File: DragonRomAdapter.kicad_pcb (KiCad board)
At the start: 2 copper layers, 20.6 x 36.9 mm, 8 parts, among them J1 Conn_01x01_Male, U1 68A364, U2 74LVC1G00, U3 28C256

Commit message: tidy-up board
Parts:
- added JP2: Jumper_2_Open, Jumper:SolderJumper-2_P1.3mm_Open_TrianglePad1.0x1.5mm, F.Cu at (165.5, 64.8)
- moved R3 0.71 mm to (160.4, 85.3)
- moved JP1 0.51 mm to (166.5, 88.0)
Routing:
- net GND: track 8.63 -> 30.0 mm, vias 0 -> 2
- net ~{E17}: track 24.5 -> 35.1 mm, vias 0 -> 3
- net ~{E}: track 15.4 -> 19.8 mm, vias 0 -> 1
- net Net-(JP1-Pad1): track 3.44 -> 2.93 mm
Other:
- board text added: "Dragon ROM adapter"
- board text added: "created by Julian Brown"

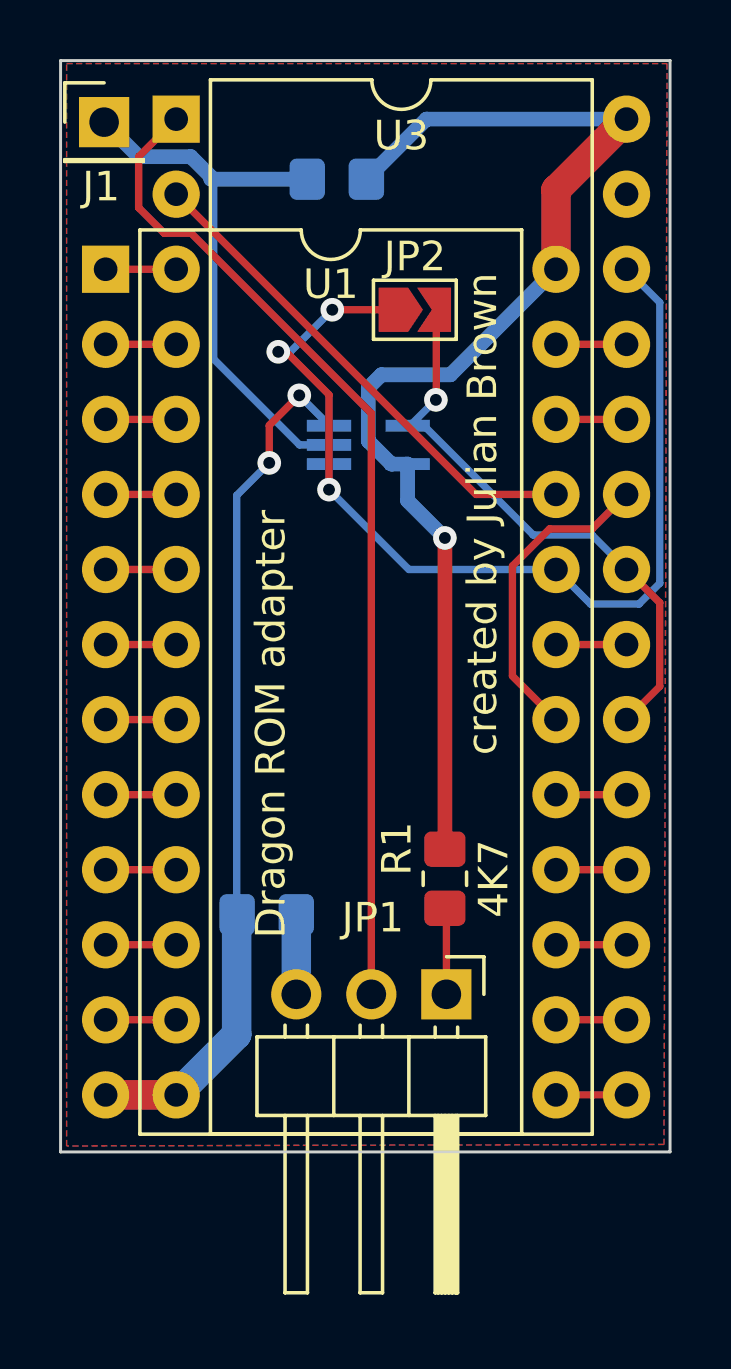
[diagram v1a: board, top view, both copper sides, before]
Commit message: reduce size of board to fit some main boards
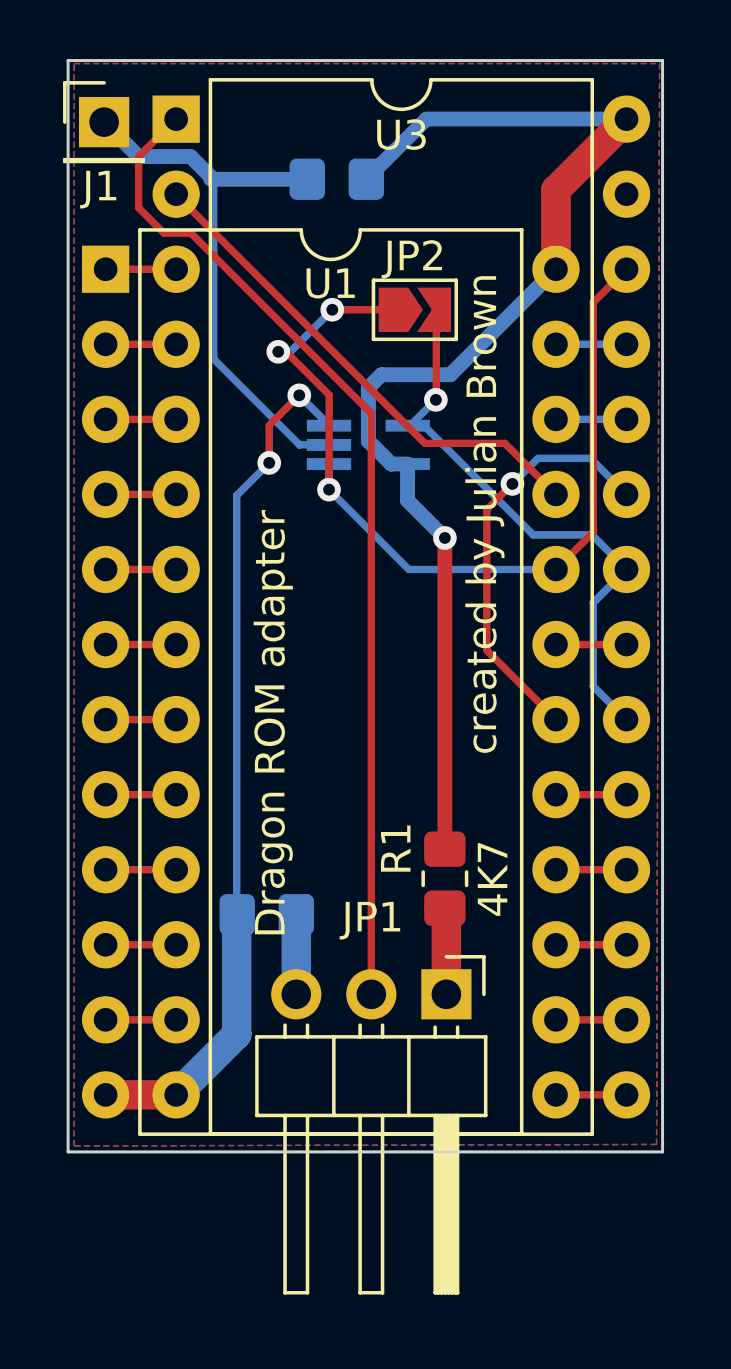
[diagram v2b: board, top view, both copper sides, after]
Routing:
- net ~{E17}: track 35.1 -> 30.8 mm
- net A11: track 10.7 -> 14.0 mm, vias 0 -> 1
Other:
- board size 20.6 x 36.9 mm -> 20.1 x 36.9 mm
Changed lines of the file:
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@@
     )
   )
-  (gr_rect (start 153.4668 56.388) (end 174.0916 93.3196) (layer "Edge.Cuts") (width 0.1) (fill none))
+  (gr_rect (start 153.7208 56.388) (end 173.8376 93.3196) (layer "Edge.Cuts") (width 0.1) (fill none))
   (gr_text "created by Julian Brown" (at 167.7416 71.7296 90) (layer "F.SilkS")
     (effects (font (size 1 1) (thickness 0.15)))
@@
   (segment (start 170.2308 81.2292) (end 172.6034 81.2292) (width 0.25) (layer "F.Cu") (net 17))
   (segment (start 172.6034 81.2292) (end 172.6134 81.2392) (width 0.25) (layer "F.Cu") (net 17))
-  (segment (start 168.7576 73.4921) (end 168.7576 77.216) (width 0.25) (layer "F.Cu") (net 18))
-  (segment (start 168.7576 77.216) (end 170.2308 78.6892) (width 0.25) (layer "F.Cu") (net 18))
-  (segment (start 171.455 72.2376) (end 170.0121 72.2376) (width 0.25) (layer "F.Cu") (net 18))
-  (segment (start 172.6134 71.0792) (end 171.455 72.2376) (width 0.25) (layer "F.Cu") (net 18))
-  (segment (start 170.0121 72.2376) (end 168.7576 73.4921) (width 0.25) (layer "F.Cu") (net 18))
+  (segment (start 167.894 71.5772) (end 167.894 76.3524) (width 0.25) (layer "F.Cu") (net 18))
+  (segment (start 167.894 76.3524) (end 170.2308 78.6892) (width 0.25) (layer "F.Cu") (net 18))
+  (segment (start 168.7576 70.7136) (end 167.894 71.5772) (width 0.25) (layer "F.Cu") (net 18))
+  (via (at 168.7576 70.7136) (size 0.8) (drill 0.4) (layers "F.Cu" "B.Cu") (net 18))
+  (segment (start 168.7576 70.7136) (end 169.6212 69.85) (width 0.25) (layer "B.Cu") (net 18))
+  (segment (start 169.6212 69.85) (end 171.3992 69.85) (width 0.25) (layer "B.Cu") (net 18))
+  (segment (start 171.3992 69.85) (end 172.6184 71.0692) (width 0.25) (layer "B.Cu") (net 18))
   (segment (start 170.2308 76.1492) (end 172.6034 76.1492) (width 0.25) (layer "F.Cu") (net 19))
   (segment (start 172.6034 76.1492) (end 172.6134 76.1592) (width 0.25) (layer "F.Cu") (net 19))
-  (segment (start 173.742911 74.733711) (end 173.742911 77.564689) (width 0.25) (layer "F.Cu") (net 20))
-  (segment (start 172.6184 73.6092) (end 173.742911 74.733711) (width 0.25) (layer "F.Cu") (net 20))
-  (segment (start 173.742911 77.564689) (end 172.6184 78.6892) (width 0.25) (layer "F.Cu") (net 20))
   (segment (start 166.1806 67.855389) (end 166.1806 64.8208) (width 0.25) (layer "F.Cu") (net 20))
   (segment (start 166.1668 67.869189) (end 166.1806 67.855389) (width 0.25) (layer "F.Cu") (net 20))
   (via (at 166.1668 67.869189) (size 0.8) (drill 0.4) (layers "F.Cu" "B.Cu") (net 20))
+  (segment (start 171.4934 74.7342) (end 172.6184 73.6092) (width 0.25) (layer "B.Cu") (net 20))
+  (segment (start 172.6184 78.6892) (end 171.4934 77.5642) (width 0.25) (layer "B.Cu") (net 20))
   (segment (start 165.2108 68.7428) (end 165.7608 68.7428) (width 0.25) (layer "B.Cu") (net 20))
   (segment (start 171.45 72.4408) (end 172.6184 73.6092) (width 0.25) (layer "B.Cu") (net 20))
@@
   (segment (start 165.293189 68.7428) (end 166.1668 67.869189) (width 0.25) (layer "B.Cu") (net 20))
   (segment (start 169.4588 72.4408) (end 171.45 72.4408) (width 0.25) (layer "B.Cu") (net 20))
-  (segment (start 170.2308 71.0692) (end 167.5234 71.0692) (width 0.25) (layer "F.Cu") (net 21))
-  (segment (start 167.5234 71.0692) (end 157.3734 60.9192) (width 0.25) (layer "F.Cu") (net 21))
-  (segment (start 170.2308 68.5292) (end 172.6034 68.5292) (width 0.25) (layer "F.Cu") (net 22))
-  (segment (start 172.6034 68.5292) (end 172.6134 68.5392) (width 0.25) (layer "F.Cu") (net 22))
-  (segment (start 172.6034 65.9892) (end 172.6134 65.9992) (width 0.25) (layer "F.Cu") (net 23))
-  (segment (start 170.2308 65.9892) (end 172.6034 65.9892) (width 0.25) (layer "F.Cu") (net 23))
+  (segment (start 171.4934 77.5642) (end 171.4934 74.7342) (width 0.25) (layer "B.Cu") (net 20))
+  (segment (start 165.7962 69.342) (end 157.3734 60.9192) (width 0.25) (layer "F.Cu") (net 21))
+  (segment (start 170.2308 71.0692) (end 168.5036 69.342) (width 0.25) (layer "F.Cu") (net 21))
+  (segment (start 168.5036 69.342) (end 165.7962 69.342) (width 0.25) (layer "F.Cu") (net 21))
+  (segment (start 170.2308 68.5292) (end 172.6184 68.5292) (width 0.25) (layer "B.Cu") (net 22))
+  (segment (start 170.2308 65.9892) (end 172.6184 65.9892) (width 0.25) (layer "B.Cu") (net 23))
   (segment (start 170.2308 63.4492) (end 170.2308 60.7618) (width 1) (layer "F.Cu") (net 24))
   (segment (start 166.4716 72.5424) (end 166.4716 83.074) (width 0.5) (layer "F.Cu") (net 24))
@@
   (segment (start 161.5508 69.3928) (end 162.5508 69.3928) (width 0.25) (layer "B.Cu") (net 25))
   (segment (start 166.4716 85.074) (end 166.5224 85.1248) (width 0.25) (layer "F.Cu") (net 26))
-  (segment (start 166.5224 85.1248) (end 166.5224 87.9856) (width 0.25) (layer "F.Cu") (net 26))
+  (segment (start 166.5224 85.1248) (end 166.5224 87.9856) (width 1) (layer "F.Cu") (net 26))
   (segment (start 156.1084 61.3664) (end 156.972 62.23) (width 0.25) (layer "F.Cu") (net 27))
   (segment (start 157.3784 58.3692) (end 156.1084 59.6392) (width 0.25) (layer "F.Cu") (net 27))
@@
   (segment (start 156.1084 59.6392) (end 156.1084 61.3664) (width 0.25) (layer "F.Cu") (net 27))
   (segment (start 163.9824 68.326) (end 163.9824 87.9856) (width 0.25) (layer "F.Cu") (net 27))
+  (segment (start 171.4934 64.5742) (end 171.4934 72.3466) (width 0.25) (layer "F.Cu") (net 28))
+  (segment (start 171.4934 72.3466) (end 170.2308 73.6092) (width 0.25) (layer "F.Cu") (net 28))
   (segment (start 162.6616 64.8208) (end 164.7306 64.8208) (width 0.25) (layer "F.Cu") (net 28))
+  (segment (start 172.6184 63.4492) (end 171.4934 64.5742) (width 0.25) (layer "F.Cu") (net 28))
   (segment (start 161.095414 66.2432) (end 160.8328 66.2432) (width 0.25) (layer "F.Cu") (net 28))
   (segment (start 162.5508 67.698586) (end 161.095414 66.2432) (width 0.25) (layer "F.Cu") (net 28))
@@
   (via (at 162.5508 70.9076) (size 0.8) (drill 0.4) (layers "F.Cu" "B.Cu") (net 28))
   (segment (start 162.5508 70.0428) (end 162.5508 70.9076) (width 0.25) (layer "B.Cu") (net 28))
-  (segment (start 173.742911 64.573711) (end 173.742911 74.074989) (width 0.25) (layer "B.Cu") (net 28))
-  (segment (start 173.742911 74.074989) (end 173.0403 74.7776) (width 0.25) (layer "B.Cu") (net 28))
-  (segment (start 172.6184 63.4492) (end 173.742911 64.573711) (width 0.25) (layer "B.Cu") (net 28))
-  (segment (start 171.3992 74.7776) (end 170.2308 73.6092) (width 0.25) (layer "B.Cu") (net 28))
-  (segment (start 173.0403 74.7776) (end 171.3992 74.7776) (width 0.25) (layer "B.Cu") (net 28))
   (segment (start 162.5508 70.9076) (end 165.2524 73.6092) (width 0.25) (layer "B.Cu") (net 28))
   (segment (start 161.2392 66.2432) (end 162.6616 64.8208) (width 0.25) (layer "B.Cu") (net 28))
@@
     (polygon
       (pts
-        (xy 173.888789 93.066309)
-        (xy 153.670392 93.116401)
-        (xy 153.670011 56.489611)
-        (xy 173.990008 56.490319)
+        (xy 173.634791 93.065605)
+        (xy 153.924392 93.116397)
+        (xy 153.924011 56.489607)
+        (xy 173.73601 56.489615)
       )
     )

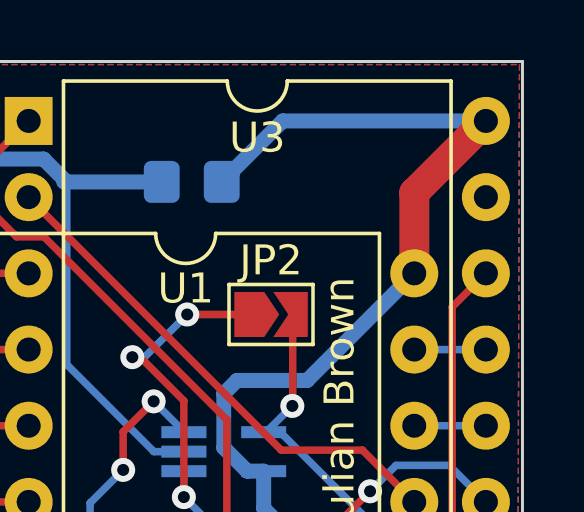
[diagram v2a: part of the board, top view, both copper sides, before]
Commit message: use acht logic instead of LVC
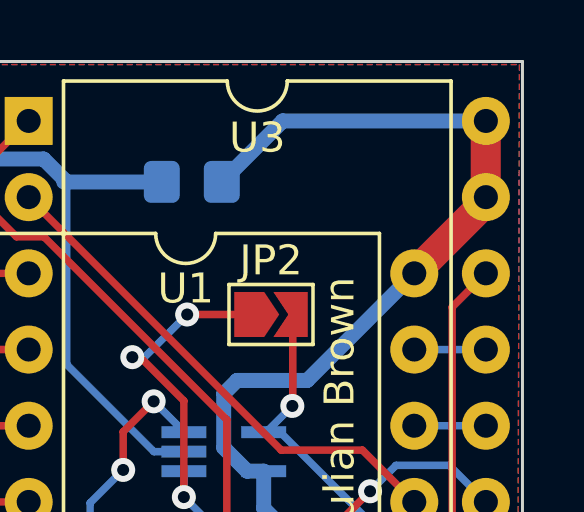
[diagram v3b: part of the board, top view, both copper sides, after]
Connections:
- U3 pad 27: unconnected-(U3-Pad27) -> +5V
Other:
- board text added: "A13"
- board text added: "~{CS}"
- board text added: "~{OE}"
- board text added: "~{WE}"
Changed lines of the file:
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@@
   (net 27 "A14")
   (net 28 "~{E17}")
-  (net 29 "unconnected-(U3-Pad27)")
-  (net 30 "Net-(JP1-Pad3)")
+  (net 29 "Net-(JP1-Pad3)")
   (footprint "Jumper:SolderJumper-2_P1.3mm_Open_TrianglePad1.0x1.5mm" (layer "F.Cu")
     (at 165.4556 64.8208)
@@
       (net 28 "~{E17}") (pinfunction "A13") (pintype "input"))
     (pad "27" thru_hole oval (at 15.24 2.54) (size 1.6 1.6) (drill 0.8) (layers *.Cu *.Mask)
-      (net 29 "unconnected-(U3-Pad27)") (pinfunction "~{WE}") (pintype "input+no_connect"))
+      (net 24 "+5V") (pinfunction "~{WE}") (pintype "input"))
     (pad "28" thru_hole oval (at 15.24 0) (size 1.6 1.6) (drill 0.8) (layers *.Cu *.Mask)
       (net 24 "+5V") (pinfunction "VCC") (pintype "power_in"))
@@
       (net 27 "A14") (pinfunction "C") (pintype "input"))
     (pad "3" thru_hole oval (at 0 5.08 270) (size 1.7 1.7) (drill 1) (layers *.Cu *.Mask)
-      (net 30 "Net-(JP1-Pad3)") (pinfunction "B") (pintype "passive"))
+      (net 29 "Net-(JP1-Pad3)") (pinfunction "B") (pintype "passive"))
     (model "${KICAD6_3DMODEL_DIR}/Connector_PinHeader_2.54mm.3dshapes/PinHeader_1x03_P2.54mm_Horizontal.wrl"
       (offset (xyz 0 0 0))
@@
       (net 12 "GND") (pintype "passive"))
     (pad "2" smd roundrect (at 1 0) (size 1.2 1.4) (layers "B.Cu" "B.Paste" "B.Mask") (roundrect_rratio 0.2083333333)
-      (net 30 "Net-(JP1-Pad3)") (pintype "passive"))
+      (net 29 "Net-(JP1-Pad3)") (pintype "passive"))
     (model "${KICAD6_3DMODEL_DIR}/Resistor_SMD.3dshapes/R_0805_2012Metric.wrl"
       (offset (xyz 0 0 0))
@@
   )
   (gr_text "Dragon ROM adapter" (at 160.5788 78.8416 90) (layer "F.SilkS")
+    (effects (font (size 1 1) (thickness 0.15)))
+  )
+  (gr_text "~{OE}" (at 175.26 73.66) (layer "User.1")
+    (effects (font (size 1 1) (thickness 0.15)))
+  )
+  (gr_text "~{CS}" (at 175.26 78.74) (layer "User.1")
+    (effects (font (size 1 1) (thickness 0.15)))
+  )
+  (gr_text "~{WE}" (at 175.26 60.96) (layer "User.1")
+    (effects (font (size 1 1) (thickness 0.15)))
+  )
+  (gr_text "A13" (at 175.514 63.5) (layer "User.1")
     (effects (font (size 1 1) (thickness 0.15)))
   )
@@
   (segment (start 170.2308 68.5292) (end 172.6184 68.5292) (width 0.25) (layer "B.Cu") (net 22))
   (segment (start 170.2308 65.9892) (end 172.6184 65.9892) (width 0.25) (layer "B.Cu") (net 23))
-  (segment (start 170.2308 63.4492) (end 170.2308 60.7618) (width 1) (layer "F.Cu") (net 24))
+  (segment (start 172.6134 61.0666) (end 172.6134 58.3792) (width 1) (layer "F.Cu") (net 24))
   (segment (start 166.4716 72.5424) (end 166.4716 83.074) (width 0.5) (layer "F.Cu") (net 24))
-  (segment (start 170.2308 60.7618) (end 172.6134 58.3792) (width 1) (layer "F.Cu") (net 24))
+  (segment (start 170.2308 63.4492) (end 172.6134 61.0666) (width 1) (layer "F.Cu") (net 24))
   (via (at 166.4716 72.5424) (size 0.8) (drill 0.4) (layers "F.Cu" "B.Cu") (net 24))
   (segment (start 163.8808 69.2628) (end 164.6608 70.0428) (width 0.5) (layer "B.Cu") (net 24))
@@
   (segment (start 165.2524 73.6092) (end 170.2308 73.6092) (width 0.25) (layer "B.Cu") (net 28))
   (segment (start 160.8328 66.2432) (end 161.2392 66.2432) (width 0.25) (layer "B.Cu") (net 28))
-  (segment (start 161.4424 85.2932) (end 161.4424 87.9856) (width 1) (layer "B.Cu") (net 30))
+  (segment (start 161.4424 85.2932) (end 161.4424 87.9856) (width 1) (layer "B.Cu") (net 29))
   (zone (net 12) (net_name "GND") (layers F&B.Cu) (hatch edge 0.508)
     (connect_pads (clearance 0.508))

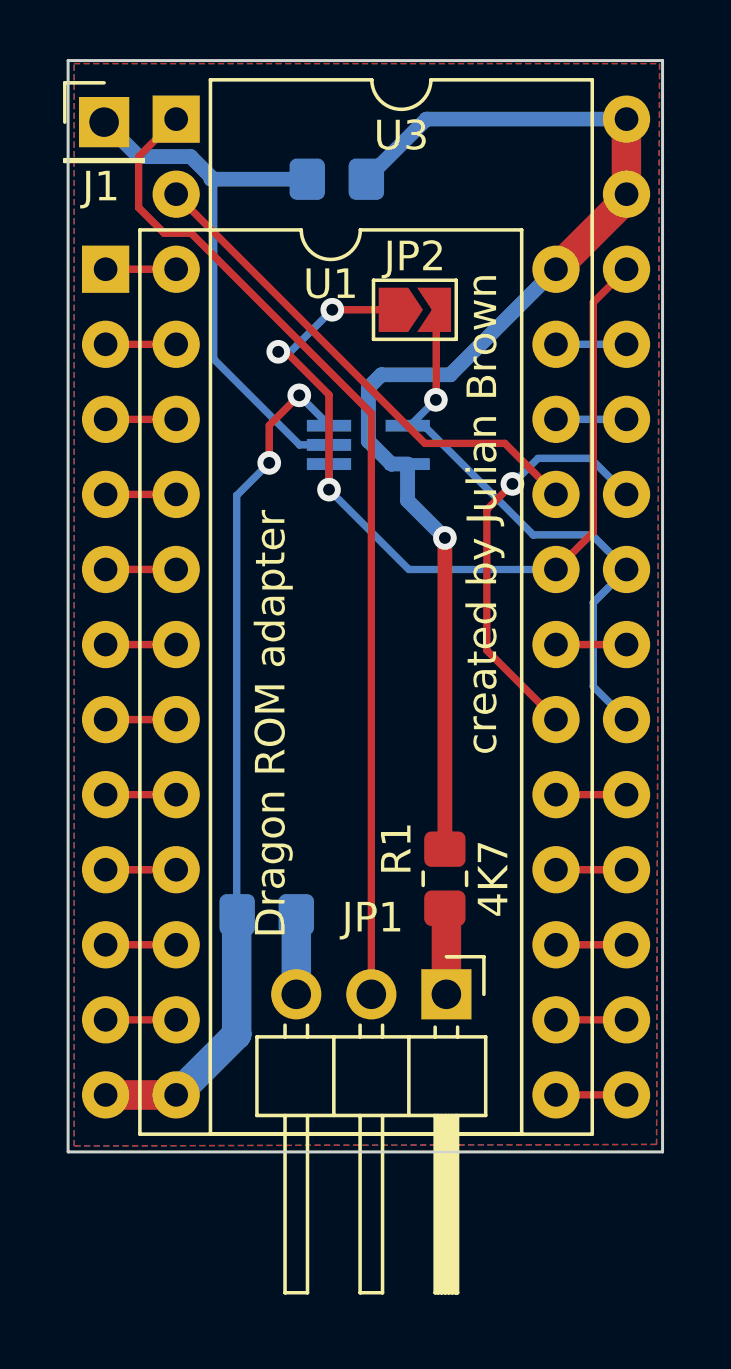
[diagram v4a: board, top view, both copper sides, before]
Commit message: make adapter compatible with 28c and 27c roms
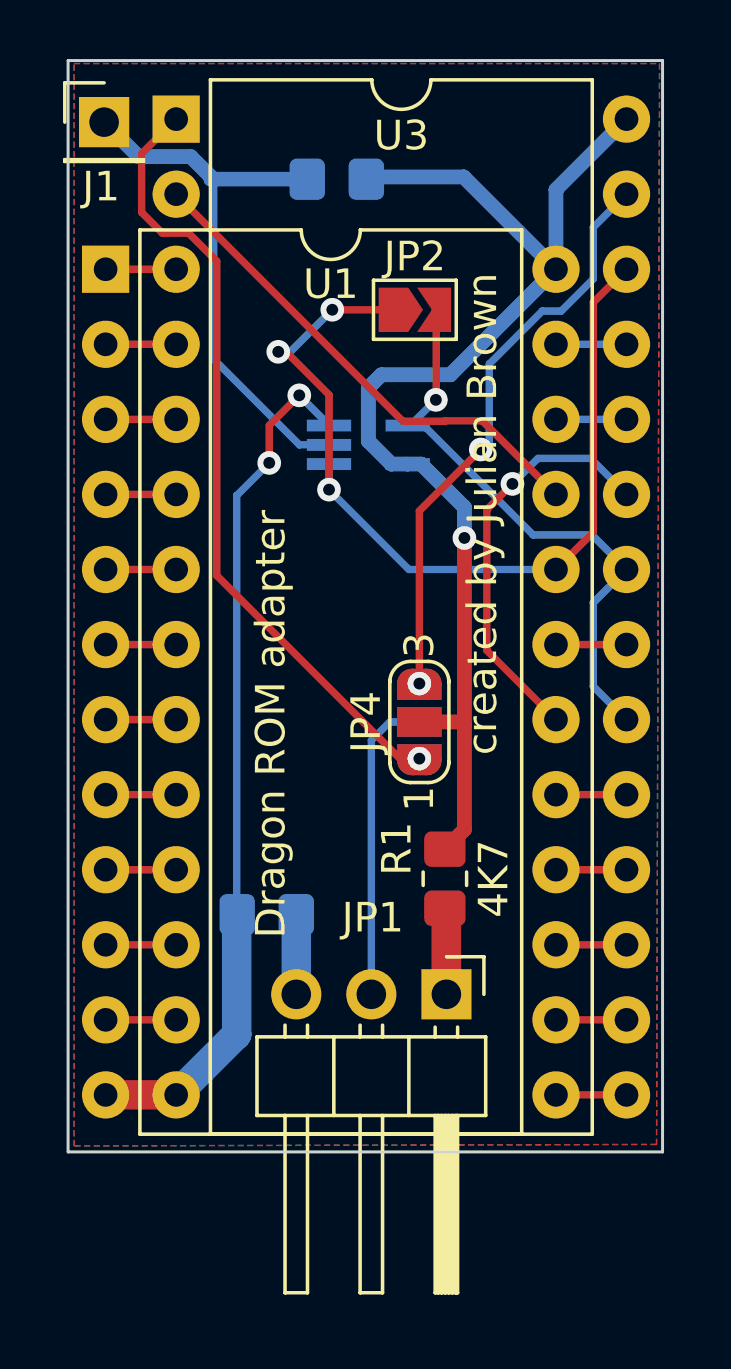
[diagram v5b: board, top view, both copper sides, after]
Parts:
- added JP3: SolderJumper_3_Open, Jumper:SolderJumper-3_P1.3mm_Open_RoundedPad1.0x1.5mm_NumberLabels, B.Cu at (165.6, 78.8)
- added JP4: SolderJumper_3_Open, Jumper:SolderJumper-3_P1.3mm_Open_RoundedPad1.0x1.5mm_NumberLabels, F.Cu at (165.6, 78.8)
- U2: value 74LVC1G00 -> 74ACHT1G00
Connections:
- U3 pad 1: A14 -> SA14-1
- U3 pad 27: +5V -> SA14-27
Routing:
- net SA14-1: track 0.00 -> 27.0 mm, vias 0 -> 1
- net A14: track 33.9 -> 10.5 mm
- net SA14-27: track 0.00 -> 19.8 mm, vias 0 -> 2
